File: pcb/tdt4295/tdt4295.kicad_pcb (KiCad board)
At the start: 6 copper layers, 184 parts, among them J101 ARM 20 Pin Debug Header, J102 MCU USART1 Header, J103 DM1AA-SF-PEJ(21), J104 MCU GPIO Header, J301 FPGA__debug, J501 618015330923, J502 FPGA GPIO, P201 690-005-299-043, U101 EFM32GG12B810F1024GQ64, U102 COM-09032 Joystick, U103 COM-09032 Joystick, U201 PHDMI2AB4, U202 TPS54294, U203 TPS54294, U301 S25FL127SABMFV101, U302 NUP4114UCW1T2G, U303 XC7A100T-FTG256-tdt4295, U501 NUP4114UCW1T2G, U502 NUP4114UCW1T2G, U503 NUP4114UCW1T2G, U504 NUP4114UCW1T2G, U601 DSC1001AL5-100.0000, Y101 48MHz

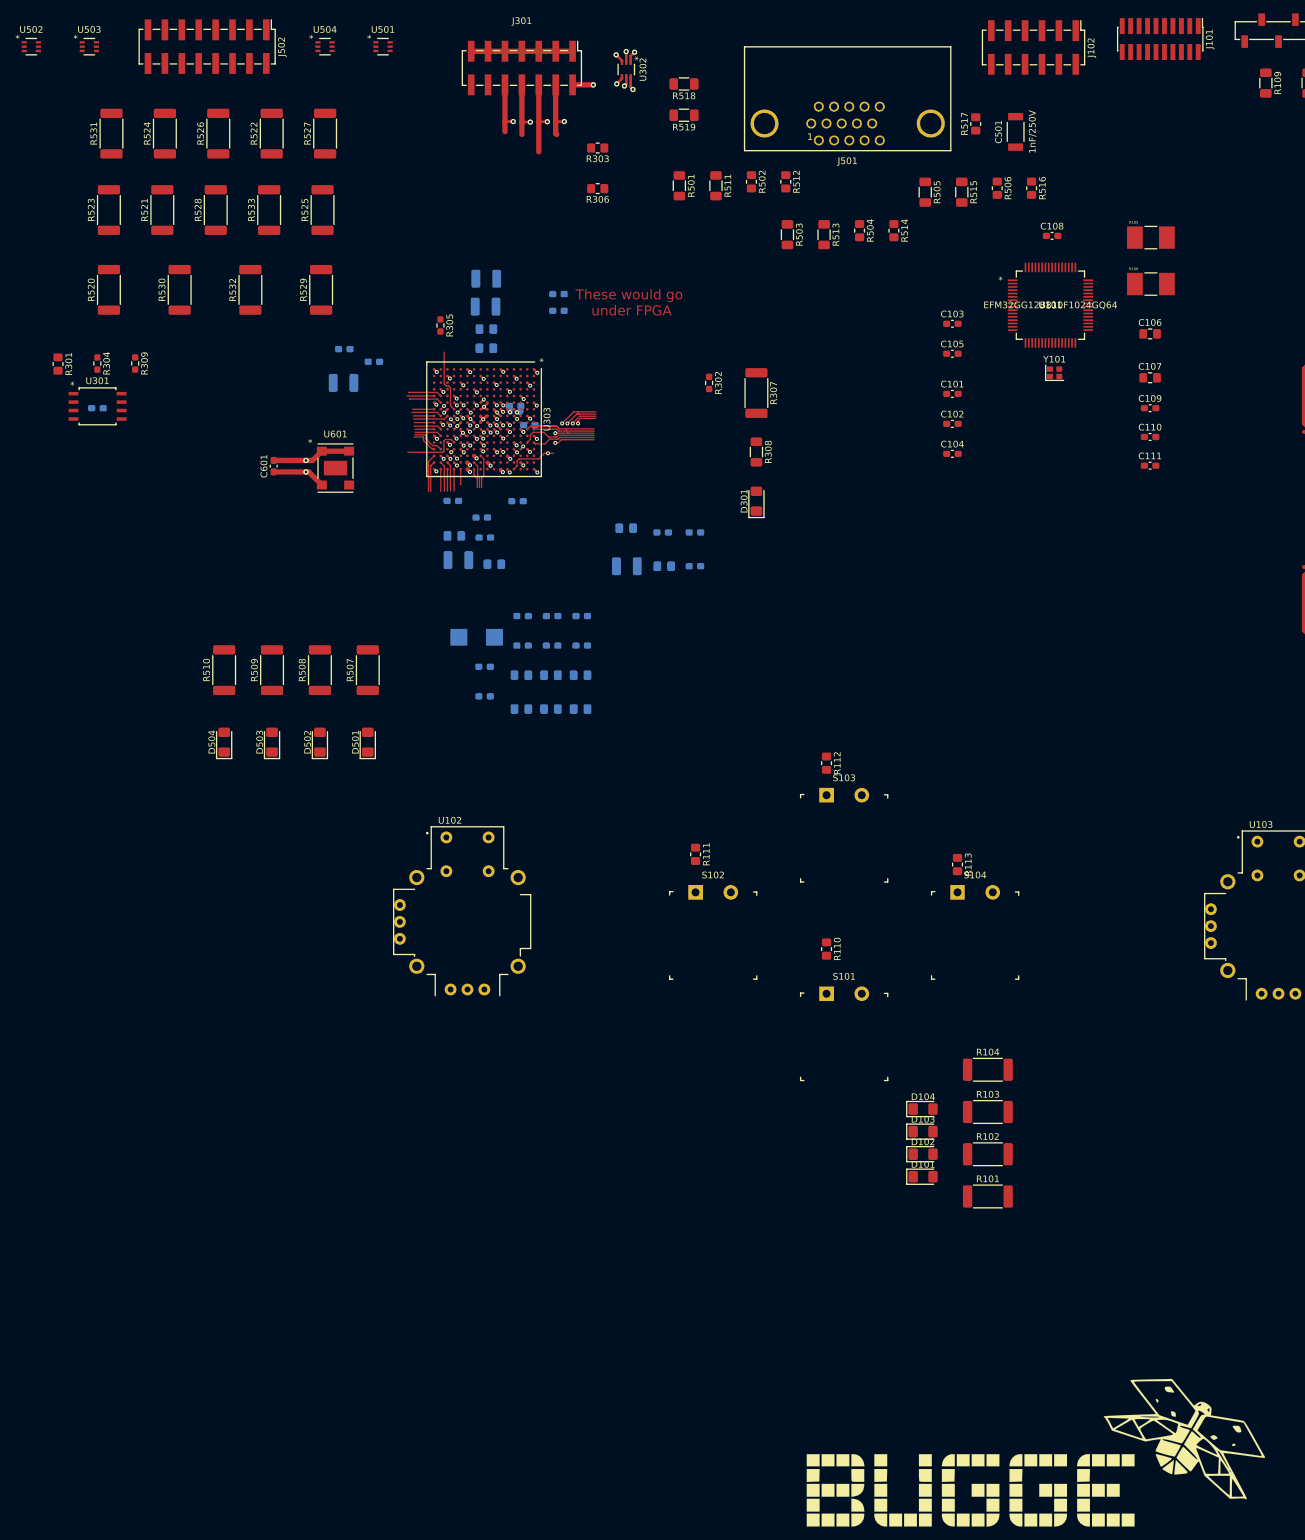
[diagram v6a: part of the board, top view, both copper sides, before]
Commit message: draw most pinouts for FPGA, place capacitors
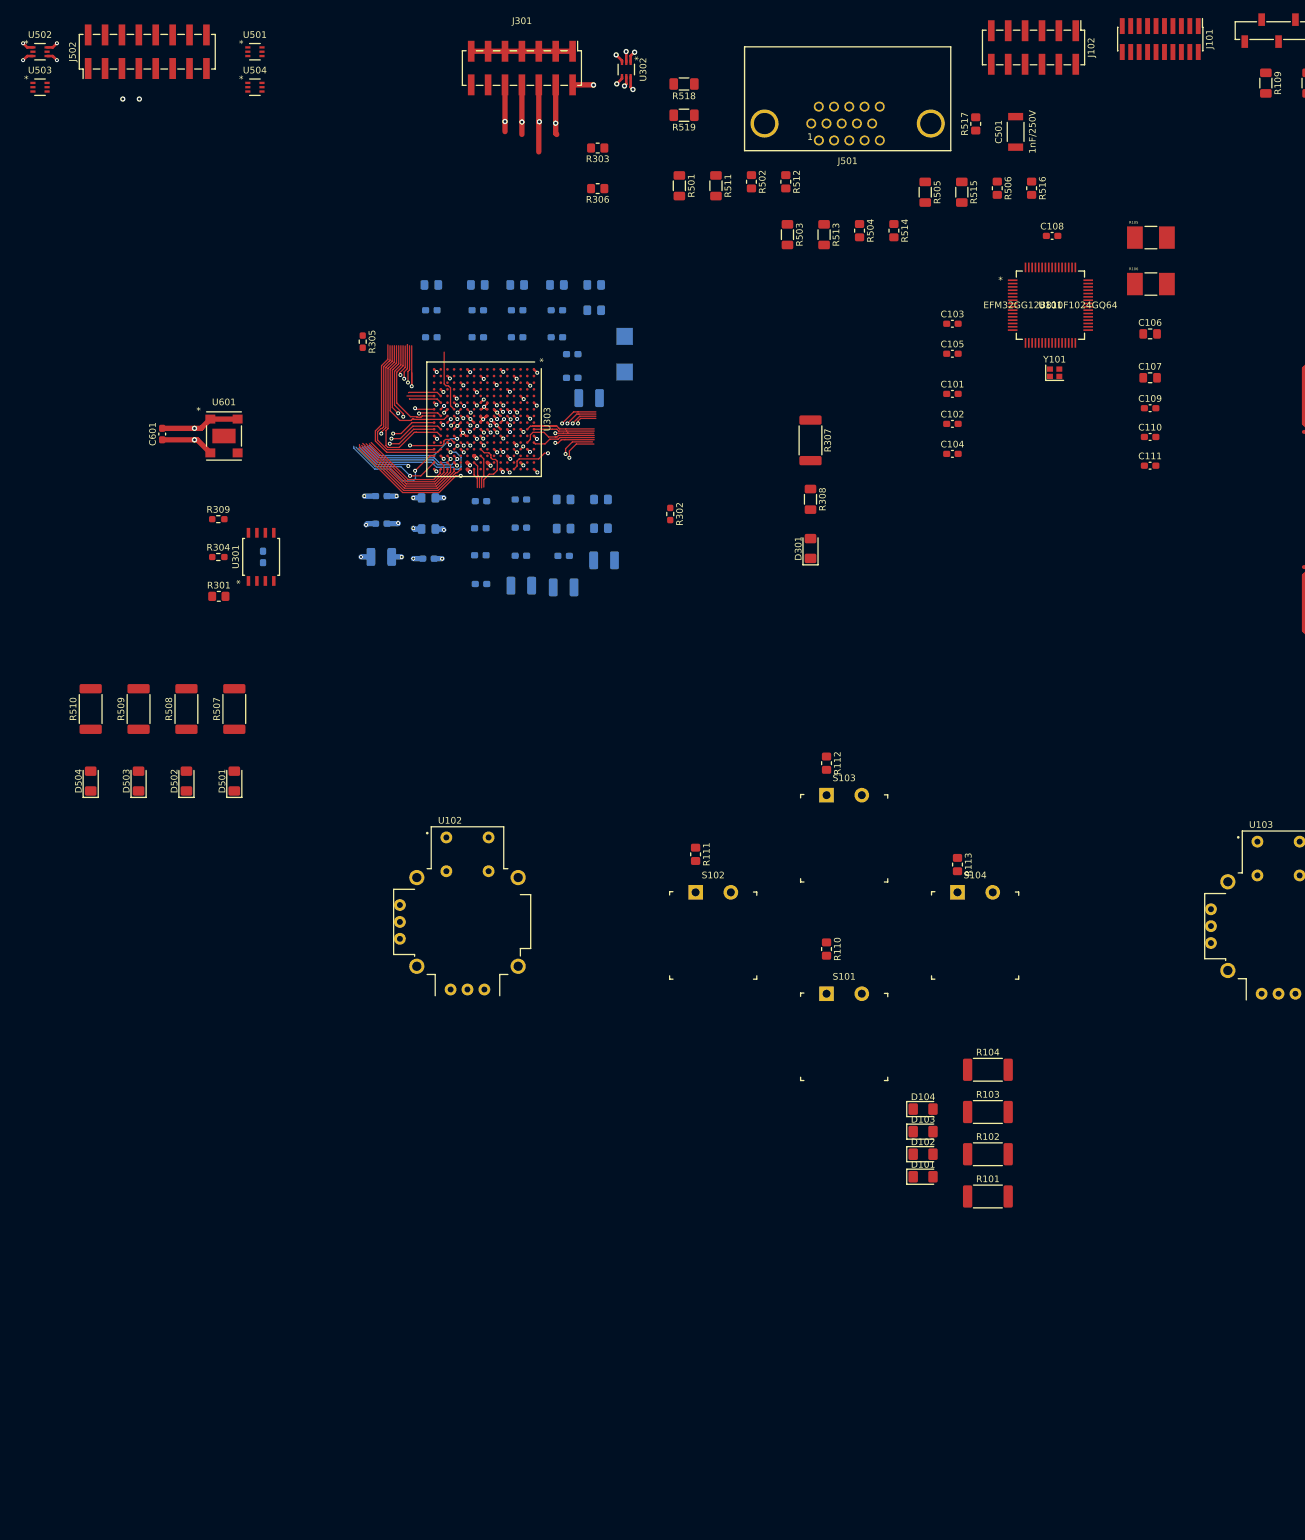
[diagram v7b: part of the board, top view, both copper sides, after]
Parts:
- removed G***: LOGO, Graphics:buggelogo_inverted
- removed R520, R521, R522, R523, R524, R525, R526, R527, R528, R529, R530, R531, R532, R533: 200, Resistor_SMD:R_2512_6332Metric_Pad1.40x3.35mm_HandSolder
- moved C307 65.6 mm to (90.5, 54.1)
- moved C304 65.2 mm to (83.5, 54.1)
- moved C305 64.0 mm to (96.4, 54.1)
- moved C312 58.7 mm to (108.0, 54.1)
- moved C310 58.7 mm to (102.3, 54.1)
- moved C309 55.9 mm to (108.0, 57.9)
- moved C324 49.7 mm to (104.6, 68.1)
- moved C326 48.8 mm to (104.6, 64.5)
- moved C313 48.3 mm to (83.5, 62.0)
- moved C303 48.0 mm to (112.5, 64.5), turned to 270 degrees
- moved C318 48.0 mm to (83.5, 57.9)
- moved C302 47.8 mm to (103.4, 99.6)
- moved C314 47.7 mm to (90.5, 62.0)
- moved C325 47.5 mm to (75.9, 85.9)
- moved C316 47.4 mm to (96.4, 62.0)
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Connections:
- J101 pad 11: Net-(J101-Pad11) -> (no net)
- J101 pad 17: Net-(J101-Pad17) -> (no net)
- J101 pad 19: Net-(J101-Pad19) -> (no net)
- J101 pad 2: Net-(J101-Pad2) -> (no net)
- J101 pad 3: Net-(J101-Pad3) -> (no net)
- J101 pad 5: Net-(J101-Pad5) -> (no net)
- J103 pad 12: Net-(J103-Pad12) -> (no net)
- J103 pad 13: Net-(J103-Pad13) -> (no net)
- J104 pad 5: Net-(J104-Pad5) -> (no net)
- J104 pad 6: Net-(J104-Pad6) -> (no net)
- J301 pad 12: Net-(J301-Pad12) -> (no net)
- J301 pad 14: Net-(J301-Pad14) -> (no net)
- J501 pad 11: Net-(J501-Pad11) -> (no net)
- J501 pad 12: Net-(J501-Pad12) -> (no net)
- J501 pad 15: Net-(J501-Pad15) -> (no net)
- J501 pad 4: Net-(J501-Pad4) -> (no net)
- J501 pad 9: Net-(J501-Pad9) -> (no net)
- J502 pad 1: Net-(J502-Pad1) -> FPGA_EXT_IO0
- J502 pad 10: Net-(J502-Pad10) -> FPGA_EXT_IO11
- J502 pad 11: Net-(J502-Pad11) -> FPGA_EXT_IO5
- J502 pad 12: Net-(J502-Pad12) -> FPGA_EXT_IO12
- J502 pad 13: Net-(J502-Pad13) -> FPGA_EXT_IO6
- J502 pad 14: Net-(J502-Pad14) -> FPGA_EXT_IO13
- J502 pad 2: Net-(J502-Pad2) -> FPGA_EXT_IO7
- J502 pad 3: Net-(J502-Pad3) -> FPGA_EXT_IO1
- J502 pad 4: Net-(J502-Pad4) -> FPGA_EXT_IO8
- J502 pad 5: Net-(J502-Pad5) -> FPGA_EXT_IO2
- J502 pad 6: Net-(J502-Pad6) -> FPGA_EXT_IO9
- J502 pad 7: Net-(J502-Pad7) -> FPGA_EXT_IO3
- J502 pad 8: Net-(J502-Pad8) -> FPGA_EXT_IO10
- J502 pad 9: Net-(J502-Pad9) -> FPGA_EXT_IO4
- P201 pad 4: Net-(P201-Pad4) -> (no net)
- U101 pad 37: Net-(U101-Pad37) -> (no net)
- U101 pad 45: Net-(U101-Pad45) -> (no net)
- U102 pad B1A: Net-(U102-PadB1A) -> (no net)
- U102 pad B2A: Net-(U102-PadB2A) -> (no net)
- U103 pad B1A: Net-(U103-PadB1A) -> (no net)
- U103 pad B2A: Net-(U103-PadB2A) -> (no net)
- U201 pad 10: Net-(U201-Pad10) -> (no net)
- U201 pad 5: Net-(U201-Pad5) -> (no net)
- U201 pad 6: Net-(U201-Pad6) -> (no net)
- U201 pad 7: Net-(U201-Pad7) -> (no net)
- U201 pad 9: Net-(U201-Pad9) -> (no net)
- U202 pad 2: Net-(U202-Pad2) -> (no net)
- U202 pad 3: Net-(U202-Pad3) -> (no net)
- U202 pad 6: Net-(U202-Pad6) -> (no net)
- U202 pad 7: Net-(U202-Pad7) -> (no net)
- U203 pad 11: Net-(U203-Pad11) -> (no net)
- U303 pad A13: Net-(U303-PadA13) -> (no net)
- U303 pad A14: Net-(U303-PadA14) -> (no net)
- U303 pad A15: Net-(U303-PadA15) -> (no net)
- U303 pad A8: Net-(U303-PadA8) -> (no net)
- U303 pad A9: Net-(U303-PadA9) -> (no net)
- U303 pad B11: Net-(U303-PadB11) -> (no net)
- U303 pad B14: Net-(U303-PadB14) -> (no net)
- U303 pad B15: Net-(U303-PadB15) -> (no net)
- U303 pad B16: Net-(U303-PadB16) -> (no net)
- U303 pad B9: Net-(U303-PadB9) -> (no net)
- U303 pad C11: Net-(U303-PadC11) -> (no net)
- U303 pad C12: Net-(U303-PadC12) -> (no net)
- U303 pad C14: Net-(U303-PadC14) -> (no net)
- U303 pad C16: Net-(U303-PadC16) -> (no net)
- U303 pad C8: Net-(U303-PadC8) -> (no net)
- U303 pad C9: Net-(U303-PadC9) -> (no net)
- U303 pad D10: Net-(U303-PadD10) -> (no net)
- U303 pad D11: Net-(U303-PadD11) -> (no net)
- U303 pad D14: Net-(U303-PadD14) -> (no net)
- U303 pad D15: Net-(U303-PadD15) -> (no net)
- U303 pad D9: Net-(U303-PadD9) -> (no net)
- U303 pad E11: Net-(U303-PadE11) -> (no net)
- U303 pad E12: Net-(U303-PadE12) -> (no net)
- U303 pad E13: Net-(U303-PadE13) -> (no net)
- U303 pad E15: Net-(U303-PadE15) -> (no net)
- U303 pad F12: Net-(U303-PadF12) -> (no net)
- U303 pad F14: Net-(U303-PadF14) -> (no net)
- U303 pad F15: Net-(U303-PadF15) -> (no net)
- U303 pad G11: Net-(U303-PadG11) -> (no net)
- U303 pad G12: Net-(U303-PadG12) -> (no net)
- U303 pad G14: Net-(U303-PadG14) -> (no net)
- U303 pad G15: Net-(U303-PadG15) -> (no net)
- U303 pad G16: Net-(U303-PadG16) -> (no net)
- U303 pad H11: Net-(U303-PadH11) -> (no net)
- U303 pad H12: Net-(U303-PadH12) -> (no net)
- U303 pad H13: Net-(U303-PadH13) -> (no net)
- U303 pad H14: Net-(U303-PadH14) -> (no net)
- U303 pad H16: Net-(U303-PadH16) -> (no net)
- U303 pad J15: Net-(U303-PadJ15) -> (no net)
- U303 pad J16: Net-(U303-PadJ16) -> (no net)
- U303 pad K12: Net-(U303-PadK12) -> (no net)
- U303 pad K13: Net-(U303-PadK13) -> (no net)
- U303 pad K7: Net-(U303-PadK7) -> (no net)
- U303 pad K8: Net-(U303-PadK8) -> (no net)
- U303 pad L13: Net-(U303-PadL13) -> (no net)
- U303 pad L14: Net-(U303-PadL14) -> (no net)
- U303 pad M14: Net-(U303-PadM14) -> (no net)
- U303 pad M15: Net-(U303-PadM15) -> (no net)
- U303 pad P10: Net-(U303-PadP10) -> (no net)
- U303 pad P11: Net-(U303-PadP11) -> (no net)
- U303 pad P6: Net-(U303-PadP6) -> (no net)
- U303 pad R12: Net-(U303-PadR12) -> (no net)
- U303 pad T12: Net-(U303-PadT12) -> (no net)
- U501 pad 1: Net-(J502-Pad9) -> FPGA_EXT_IO4
- U501 pad 3: Net-(J502-Pad13) -> FPGA_EXT_IO6
- U501 pad 4: Net-(U501-Pad4) -> (no net)
- U501 pad 6: Net-(J502-Pad11) -> FPGA_EXT_IO5
- U502 pad 1: Net-(J502-Pad1) -> FPGA_EXT_IO0
- U502 pad 3: Net-(J502-Pad7) -> FPGA_EXT_IO3
- U502 pad 4: Net-(J502-Pad5) -> FPGA_EXT_IO2
- U502 pad 6: Net-(J502-Pad3) -> FPGA_EXT_IO1
- U503 pad 1: Net-(J502-Pad2) -> FPGA_EXT_IO7
- U503 pad 3: Net-(J502-Pad8) -> FPGA_EXT_IO10
- U503 pad 4: Net-(J502-Pad6) -> FPGA_EXT_IO9
- U503 pad 6: Net-(J502-Pad4) -> FPGA_EXT_IO8
- U504 pad 1: Net-(J502-Pad10) -> FPGA_EXT_IO11
- U504 pad 3: Net-(J502-Pad14) -> FPGA_EXT_IO13
- U504 pad 4: Net-(U504-Pad4) -> (no net)
- U504 pad 6: Net-(J502-Pad12) -> FPGA_EXT_IO12
- U601 pad 5: Net-(U601-Pad5) -> (no net)
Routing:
- net FPGA_EXT_IO3: track 4.48 -> 44.3 mm, vias 0 -> 2
- net FPGA_EXT_IO2: track 3.28 -> 35.1 mm, vias 0 -> 2
- net VGA_R3: track 4.09 -> 25.2 mm
- net VGA_R0: track 5.12 -> 26.0 mm
- net FPGA_EXT_IO10: track 0.00 -> 20.4 mm, vias 0 -> 1
- net VGA_R1: track 4.09 -> 24.2 mm
- net VGA_R2: track 4.17 -> 24.1 mm, vias 0 -> 2
- net FPGA_EXT_IO1: track 2.37 -> 21.3 mm, vias 0 -> 1
- net FPGA_EXT_IO0: track 7.84 -> 26.7 mm, vias 1 -> 3
- net +1V8: track 102.9 -> 120.5 mm, vias 5 -> 11
- net FPGA_EXT_IO9: track 5.05 -> 21.0 mm, vias 1 -> 2
- net VGA_G0: track 5.29 -> 19.7 mm
- net VGA_G1: track 4.55 -> 18.8 mm, vias 0 -> 2
- net Net-(U301-Pad6): track 0.00 -> 14.1 mm, vias 0 -> 1
- net VGA_G2: track 3.24 -> 16.8 mm, vias 0 -> 2
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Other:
- board text removed: "These would go under FPGA"

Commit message: more fpga routing
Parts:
- C301: moved to F.Cu
- moved D504 118.2 mm to (105.4, 35.9), turned to 270 degrees
- moved D503 109.8 mm to (98.2, 35.9), turned to 270 degrees
- moved D502 102.8 mm to (91.0, 35.9), turned to 270 degrees
- moved R510 102.0 mm to (105.4, 46.7), turned to 270 degrees
- moved D501 97.5 mm to (83.8, 35.9), turned to 270 degrees
- moved R509 92.3 mm to (98.2, 46.7), turned to 270 degrees
- moved R508 83.8 mm to (91.0, 46.7), turned to 270 degrees
- moved R507 77.2 mm to (83.8, 46.7), turned to 270 degrees
- moved R304 18.9 mm to (69.8, 99.3), turned to 90 degrees
- moved R309 15.5 mm to (65.8, 83.6)
- moved C601 15.0 mm to (58.0, 75.3)
- moved R302 14.7 mm to (106.9, 80.8), turned to 90 degrees
- moved R301 13.8 mm to (65.3, 99.3), turned to 90 degrees
- moved U601 13.0 mm to (65.2, 75.5)
- moved U301 10.3 mm to (67.3, 90.7)
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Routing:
- net GND: track 216.4 -> 255.5 mm, vias 117 -> 150
- net VGA_G1: track 18.8 -> 54.4 mm
- net VGA_B1: track 16.0 -> 51.6 mm
- net VGA_G0: track 19.7 -> 55.2 mm
- net VGA_B0: track 17.8 -> 53.3 mm
- net VGA_G2: track 16.8 -> 52.2 mm
- net VGA_B2: track 19.6 -> 54.8 mm
- net VGA_G3: track 15.6 -> 50.5 mm
- net VGA_B3: track 16.7 -> 50.2 mm
- net Net-(J501-Pad14): track 0.00 -> 23.4 mm
- net +1V0: track 107.4 -> 130.2 mm, vias 8 -> 26
- net Net-(J501-Pad13): track 0.00 -> 20.7 mm
- net +3V3: track 132.4 -> 150.0 mm, vias 16 -> 33
- net /FPGA/IOB14/GCLK100: track 7.47 -> 20.8 mm, vias 1 -> 2
- net /FPGA/IOB14/QSPI_CS: track 7.39 -> 19.9 mm
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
